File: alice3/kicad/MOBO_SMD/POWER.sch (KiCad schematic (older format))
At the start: 3 parts, among them U6 LD29080DT33R

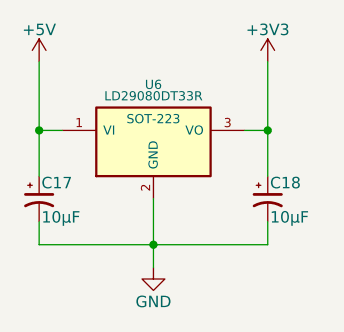
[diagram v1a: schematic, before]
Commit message: Run all address lines to ARM UART header
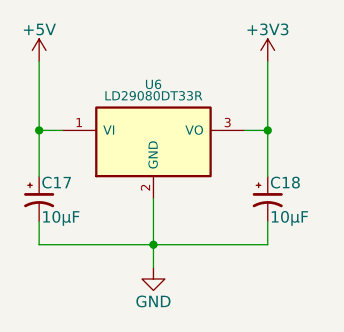
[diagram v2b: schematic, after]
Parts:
- U6: footprint SOT-223 -> TO_SOT_Packages_SMD:SOT-223
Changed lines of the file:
@@
 F 0 "U6" H 7300 1900 40  0000 C CNN
 F 1 "LD29080DT33R" H 7300 1850 40  0000 C CNN
-F 2 "SOT-223" H 7300 1750 40  0000 C CNN
+F 2 "TO_SOT_Packages_SMD:SOT-223" H 7300 1750 40  0001 C CNN
 F 3 "" H 7300 1650 60  0000 C CNN
 	1    7300 1650
@@
 $EndComp
 $Comp
-L GND #PWR54
+L GND #PWR054
 U 1 1 56BA78E3
 P 7300 2200
-F 0 "#PWR54" H 7300 1950 50  0001 C CNN
+F 0 "#PWR054" H 7300 1950 50  0001 C CNN
 F 1 "GND" H 7300 2050 50  0000 C CNN
 F 2 "" H 7300 2200 60  0000 C CNN
@@
 F 0 "C17" H 6810 1970 50  0000 L CNN
 F 1 "10µF" H 6810 1820 50  0000 L CNN
-F 2 "" H 6800 1900 60  0000 C CNN
+F 2 "" H 6800 1900 60  0001 C CNN
 F 3 "" H 6800 1900 60  0000 C CNN
 	1    6800 1900
@@
 F 0 "C18" H 7810 1970 50  0000 L CNN
 F 1 "10µF" H 7810 1820 50  0000 L CNN
-F 2 "" H 7800 1900 60  0000 C CNN
+F 2 "" H 7800 1900 60  0001 C CNN
 F 3 "" H 7800 1900 60  0000 C CNN
 	1    7800 1900
@@
 	7800 2100 7800 2000
 $Comp
-L +3V3 #PWR55
+L +3V3 #PWR055
 U 1 1 56BA7A57
 P 7800 1300
-F 0 "#PWR55" H 7800 1150 50  0001 C CNN
+F 0 "#PWR055" H 7800 1150 50  0001 C CNN
 F 1 "+3V3" H 7800 1440 50  0000 C CNN
 F 2 "" H 7800 1300 60  0000 C CNN
@@
 Connection ~ 7800 1600
 $Comp
-L +5V #PWR53
+L +5V #PWR056
 U 1 1 56BA7A9A
 P 6800 1300
-F 0 "#PWR53" H 6800 1150 50  0001 C CNN
+F 0 "#PWR056" H 6800 1150 50  0001 C CNN
 F 1 "+5V" H 6800 1440 50  0000 C CNN
 F 2 "" H 6800 1300 60  0000 C CNN

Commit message: Stab at full PCB
replace DIP36 128KB RAM with TSOP44 512KB RAM
change footprints for many components to SMD
sample PCB layout
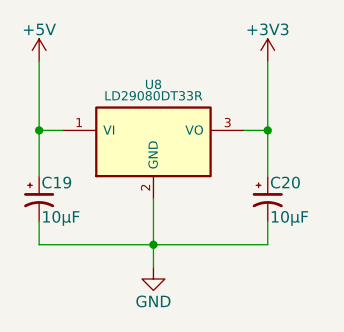
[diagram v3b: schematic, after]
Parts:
- C19: renamed from C17; footprint (none) -> Capacitors_ThroughHole:C_Radial_D5_L11_P2.5
- C20: renamed from C18; footprint (none) -> Capacitors_ThroughHole:C_Radial_D5_L11_P2.5
- renumbered U6 to U8
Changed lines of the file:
@@
 LIBS:regul
 LIBS:ldo
+LIBS:71v424s15phgi8
 LIBS:MOBO_SMD-cache
 EELAYER 25 0
@@
 $EndDescr
 $Comp
-L LD29080DT33R U6
+L LD29080DT33R U8
 U 1 1 56BA71CB
 P 7300 1650
-F 0 "U6" H 7300 1900 40  0000 C CNN
+F 0 "U8" H 7300 1900 40  0000 C CNN
 F 1 "LD29080DT33R" H 7300 1850 40  0000 C CNN
 F 2 "TO_SOT_Packages_SMD:SOT-223" H 7300 1750 40  0001 C CNN
@@
 $EndComp
 $Comp
-L GND #PWR054
+L GND #PWR058
 U 1 1 56BA78E3
 P 7300 2200
-F 0 "#PWR054" H 7300 1950 50  0001 C CNN
+F 0 "#PWR058" H 7300 1950 50  0001 C CNN
 F 1 "GND" H 7300 2050 50  0000 C CNN
 F 2 "" H 7300 2200 60  0000 C CNN
@@
 $EndComp
 $Comp
-L CP1_Small C17
+L CP1_Small C19
 U 1 1 56BA78F3
 P 6800 1900
-F 0 "C17" H 6810 1970 50  0000 L CNN
+F 0 "C19" H 6810 1970 50  0000 L CNN
 F 1 "10µF" H 6810 1820 50  0000 L CNN
-F 2 "" H 6800 1900 60  0001 C CNN
+F 2 "Capacitors_ThroughHole:C_Radial_D5_L11_P2.5" H 6800 1900 60  0001 C CNN
 F 3 "" H 6800 1900 60  0000 C CNN
 	1    6800 1900
@@
 $EndComp
 $Comp
-L CP1_Small C18
+L CP1_Small C20
 U 1 1 56BA7930
 P 7800 1900
-F 0 "C18" H 7810 1970 50  0000 L CNN
+F 0 "C20" H 7810 1970 50  0000 L CNN
 F 1 "10µF" H 7810 1820 50  0000 L CNN
-F 2 "" H 7800 1900 60  0001 C CNN
+F 2 "Capacitors_ThroughHole:C_Radial_D5_L11_P2.5" H 7800 1900 60  0001 C CNN
 F 3 "" H 7800 1900 60  0000 C CNN
 	1    7800 1900
@@
 	7800 2100 7800 2000
 $Comp
-L +3V3 #PWR055
+L +3V3 #PWR059
 U 1 1 56BA7A57
 P 7800 1300
-F 0 "#PWR055" H 7800 1150 50  0001 C CNN
+F 0 "#PWR059" H 7800 1150 50  0001 C CNN
 F 1 "+3V3" H 7800 1440 50  0000 C CNN
 F 2 "" H 7800 1300 60  0000 C CNN
@@
 Connection ~ 7800 1600
 $Comp
-L +5V #PWR056
+L +5V #PWR060
 U 1 1 56BA7A9A
 P 6800 1300
-F 0 "#PWR056" H 6800 1150 50  0001 C CNN
+F 0 "#PWR060" H 6800 1150 50  0001 C CNN
 F 1 "+5V" H 6800 1440 50  0000 C CNN
 F 2 "" H 6800 1300 60  0000 C CNN
